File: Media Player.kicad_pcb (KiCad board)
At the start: 4 copper layers, 114.3 x 68.5 mm, 142 parts, among them J1 USB_C_Receptacle_USB2.0_16P, J10 MEM2075-00-140-01-A, J40 PH2.0, J41 UART, J70 SJ-3524-SMT-TR, Q10 DMP3068L-7, Q40 DMP3068L-7, Q50 DMP3068L-7, Q70 DMP3068L-7, SW30 BOOT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

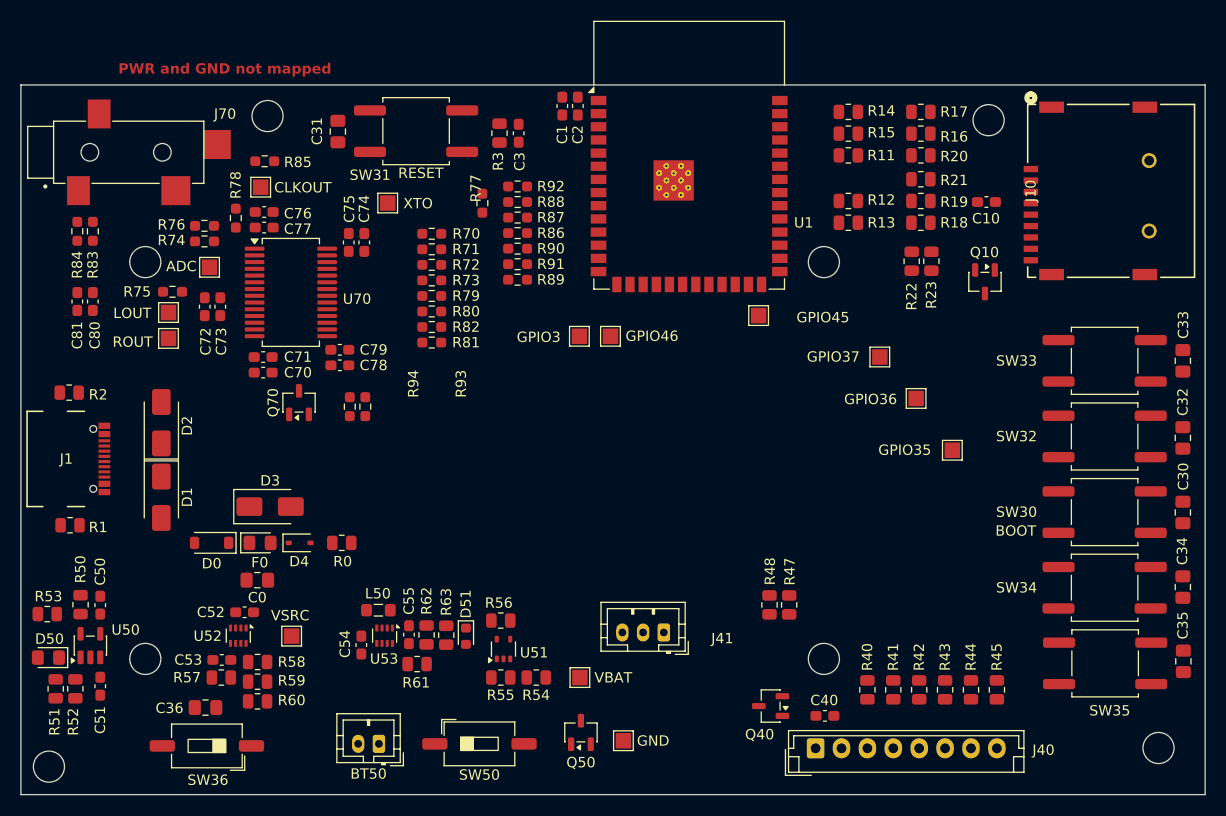
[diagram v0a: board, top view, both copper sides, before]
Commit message: JLC Design restraints
Updated design rules with JLC PCB. Combined numbers from Phils Lab and GPT for beginner friendly values (first board)
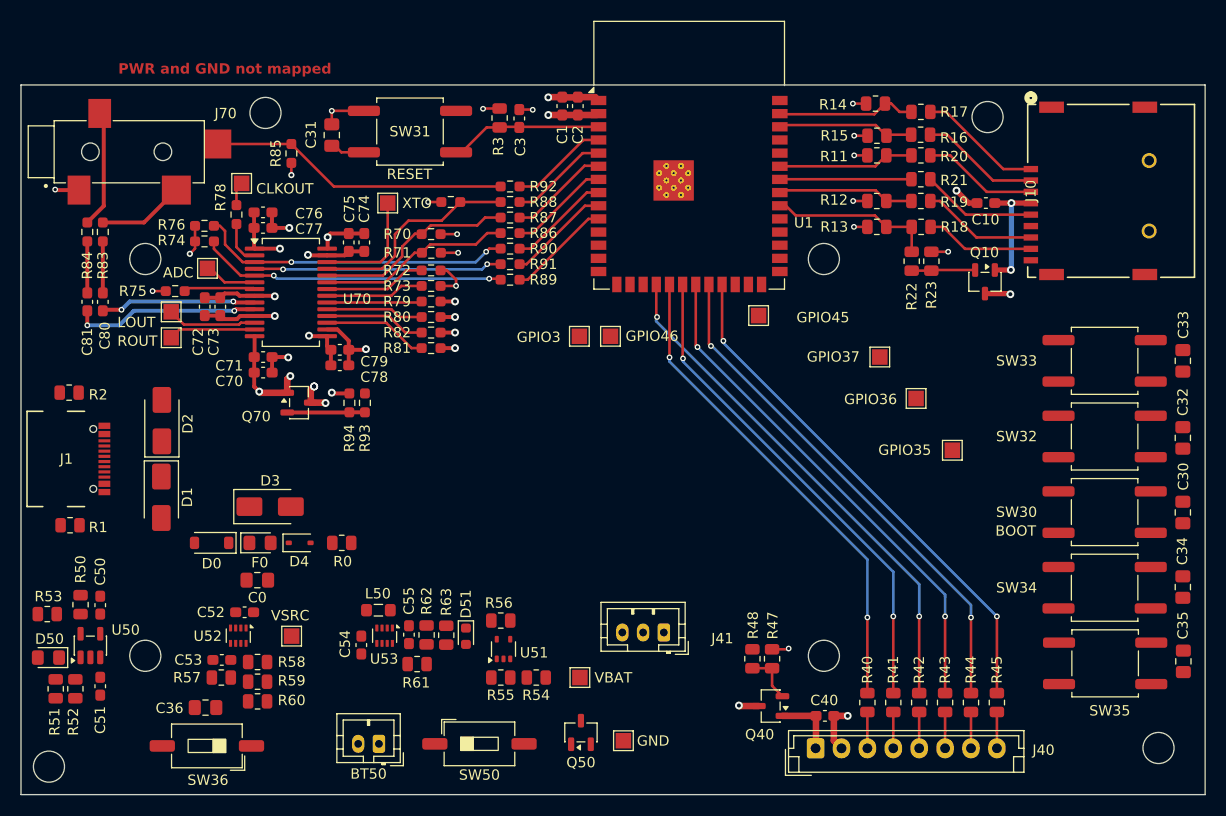
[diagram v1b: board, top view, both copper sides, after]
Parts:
- J1: value USB_C_Receptacle_USB2.0_16P -> 12402012E212A
- moved R47 5.46 mm to (158.7, 95.4)
- moved R48 5.46 mm to (156.8, 95.4)
- moved R77 3.05 mm to (127.7, 51.3), turned to 180 degrees
- moved R13 2.78 mm to (168.8, 53.7)
- moved R15 2.77 mm to (168.8, 44.9)
- moved R11 2.75 mm to (168.8, 46.8)
- moved R12 2.75 mm to (168.8, 51.2)
- moved R14 2.74 mm to (168.7, 41.8)
- moved R85 2.68 mm to (112.3, 46.6), turned to -90 degrees
- moved TP70 1.87 mm to (107.5, 49.5)
- moved R3 1.46 mm to (132.4, 43.2)
- moved C3 1.43 mm to (134.3, 43.2)
- moved R40 1.22 mm to (167.9, 99.6)
- moved R41 1.22 mm to (170.4, 99.6)
- moved R42 1.22 mm to (172.9, 99.6)
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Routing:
- net GND: track 0.00 -> 58.5 mm, vias 0 -> 19
- net /LCD_BL: track 0.00 -> 50.5 mm, vias 0 -> 2
- net /LCD_RST_n: track 0.00 -> 50.0 mm, vias 0 -> 2
- net /LCD_CS_n: track 0.00 -> 49.9 mm, vias 0 -> 2
- net /LCD_DS: track 0.00 -> 49.4 mm, vias 0 -> 2
- net /LCD_CLK: track 0.00 -> 47.9 mm, vias 0 -> 2
- net /LCD_DIN: track 0.00 -> 47.4 mm, vias 0 -> 2
- net /AudioAlt/A2_BCLK: track 0.00 -> 30.4 mm, vias 0 -> 2
- net /AudioAlt/A2_DACLRC: track 0.00 -> 29.6 mm, vias 0 -> 2
- net /AudioAlt/A2_TSW: track 0.00 -> 29.0 mm
- net /AudioAlt/AVDD: track 0.00 -> 28.6 mm, vias 0 -> 5
- net /AudioAlt/A2_DACDAT: track 0.00 -> 24.0 mm, vias 0 -> 2
- net +3V3: track 0.00 -> 23.9 mm, vias 0 -> 14
- net /AudioAlt/A2_MCLK: track 0.00 -> 20.7 mm
- net /AudioAlt/A2_SCLK: track 0.00 -> 19.6 mm
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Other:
- outline, holes or cut-outs redrawn
- board text added: "AVDD Area"
- board text added: "Am i allowed to do this? Decap is reached AFTER the pwr pin"
- board text added: "Avoid silk screen on via"
- board text added: "Design Rules are a combination of JLC, PhilsLab, and GPT values"
- board text added: "Make sure sd card signal length are +-50 mil"
- board text added: "VMID Area"
- board text added: "change size"
- board text added: "check recommended layout"

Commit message: Bucked
The Boost Buck Converter layout is from the datasheet. I'm not really sure how many via's I'll need for power since the IC is so small yet its the only source of power feeding all the other peripherals.
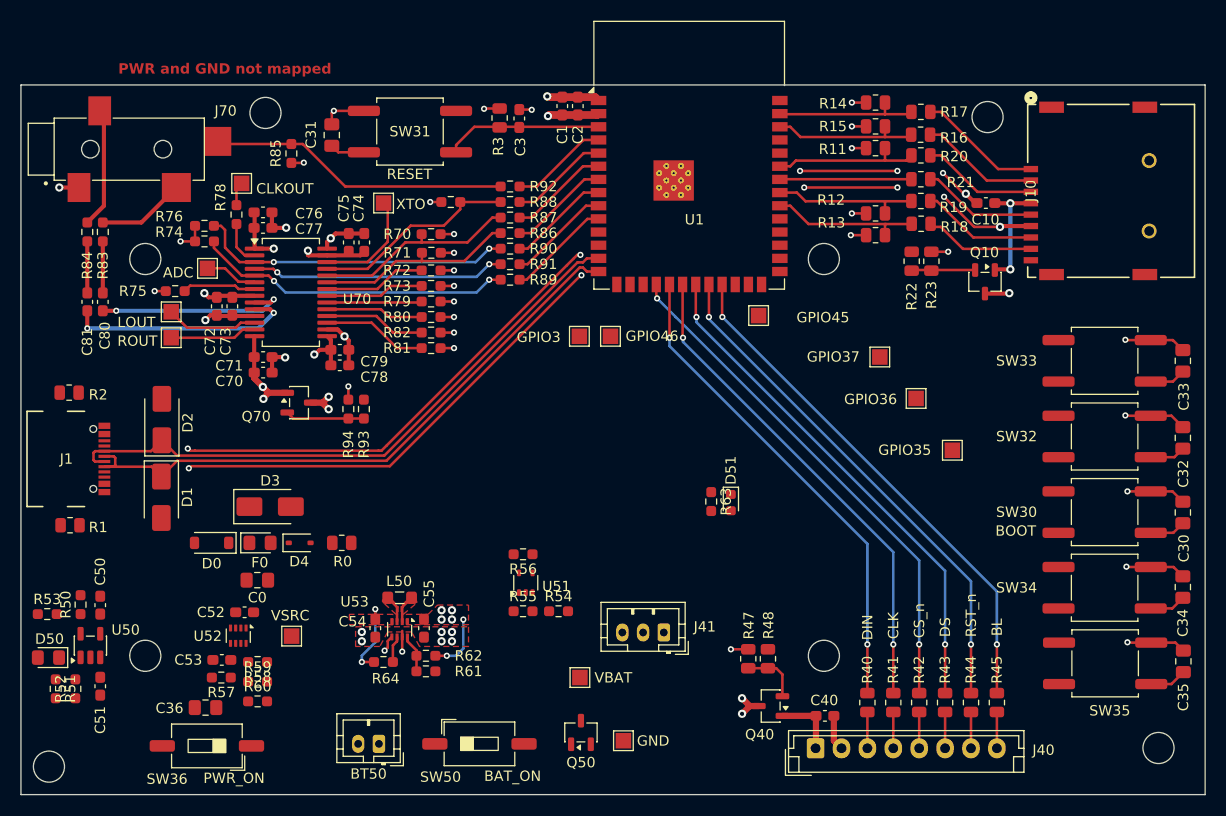
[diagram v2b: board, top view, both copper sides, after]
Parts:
- added R64: 10kΩ, Resistor_SMD:R_0603_1608Metric_Pad0.98x0.95mm_HandSolder, F.Cu at (121.2, 95.7)
- R50, R51, R52, R53, R54, R55, R56, R57, R58, R59, R60, R61, R62, R63: footprint Resistor_SMD:R_0805_2012Metric -> Resistor_SMD:R_0603_1608Metric_Pad0.98x0.95mm_HandSolder
- moved D51 28.6 mm to (154.7, 80.3)
- moved R63 28.6 mm to (152.8, 80.2)
- moved R54 6.75 mm to (138.1, 90.8)
- moved R55 6.75 mm to (134.7, 90.8)
- moved R56 6.75 mm to (134.7, 85.3)
- moved U51 6.75 mm to (134.9, 88.0)
- moved L50 2.38 mm to (122.8, 89.5)
- moved R47 2.30 mm to (156.4, 95.4)
- moved C54 2.11 mm to (120.4, 92.4)
- moved R62 2.01 mm to (125.3, 95.1), turned to 180 degrees
- moved C55 1.58 mm to (125.1, 92.4)
- moved U53 1.58 mm to (122.8, 92.5)
- moved R48 1.50 mm to (158.3, 95.4)
- moved R12 1.21 mm to (168.7, 52.4)
- moved C72 1.16 mm to (105.1, 61.4)
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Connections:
- net Net-(U53-LX1) renamed /Power/LX1
- net Net-(U53-LX2) renamed /Power/LX2
- C55 pad 1: +3.3V -> +3V3
- R62 pad 1: +3.3V -> +3V3
- R63 pad 1: +3.3V -> +3V3
- U51 pad 5: +3.3V -> +3V3
- U53 pad 1: +3.3V -> +3V3
- U53 pad 6: VSRC -> Net-(U53-MODE)
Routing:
- net GND: track 58.5 -> 204.4 mm, vias 19 -> 42
- net /USB_D-: track 0.00 -> 59.6 mm
- net /USB_D+: track 0.00 -> 59.5 mm
- net VSRC: track 0.00 -> 7.79 mm, vias 0 -> 2
- net +3V3: track 23.9 -> 30.1 mm, vias 14 -> 20
- net /AudioAlt/RHPOUT: track 18.2 -> 22.3 mm
- net /AudioAlt/LHPOUT: track 15.1 -> 18.9 mm
- net Net-(U53-FB): track 0.00 -> 3.68 mm
- net /PB3: track 0.00 -> 3.58 mm
- net /PB2: track 0.00 -> 3.52 mm
- net /PB1: track 0.00 -> 3.50 mm
- net /GPIO0: track 0.00 -> 3.48 mm
- net /AudioAlt/AVDD: track 28.6 -> 25.1 mm
- net /PB0: track 0.00 -> 3.44 mm
- net /Power/LX2: track 0.00 -> 2.67 mm
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- added copper zone on F.Cu, net +3V3
- added copper zone on F.Cu, net /Power/LX1
- added copper zone on F.Cu, net /Power/LX2
- added copper zone on F.Cu, net GND
- added copper zone on In1.Cu, net GND
- added copper zone on F.Cu, net VSRC
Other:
- board text added: "BAT_ON"
- board text added: "BL"
- board text added: "CLK"
- board text added: "CS_n"
- board text added: "DIN"
- board text added: "DS"
- board text added: "ESP asked to keep GND traces aroudn CLK, but this part near the pin also has 3v3"
- board text added: "PWR_ON"
- board text added: "RST_n"
- board text added: "Should each decap use it's own GND via?"
- board text added: "check for requirements surrounding GND and CLK"
- board text removed: "change size"

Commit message: Ideal Diode
Layout based on ds
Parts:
- moved D51 30.0 mm to (128.3, 94.5), turned to 0 degrees
- moved R63 27.5 mm to (128.4, 92.9), turned to 0 degrees
- moved C0 13.6 mm to (122.2, 84.3)
- moved J41 12.2 mm to (151.3, 104.7)
- moved R57 7.14 mm to (103.2, 90.5), turned to 0 degrees
- moved R55 5.22 mm to (135.8, 95.9)
- moved R56 5.22 mm to (135.8, 90.4)
- moved R54 5.22 mm to (139.2, 95.9)
- moved U51 5.22 mm to (136.0, 93.2)
- moved TP51 5.21 mm to (139.2, 103.7)
- moved Q50 5.21 mm to (135.1, 102.8)
- moved BT50 4.06 mm to (116.7, 103.8)
- moved SW50 4.06 mm to (126.4, 103.8)
- moved TP50 2.94 mm to (139.3, 100.0)
- moved C54 2.34 mm to (118.5, 93.8)
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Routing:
- net +3V3: track 30.1 -> 25.4 mm, vias 20 -> 19
- net Net-(U52-ST): track 0.00 -> 3.43 mm
- net /PWR_SRC: track 0.00 -> 2.77 mm, vias 0 -> 1
- net /PWR_ON_n: track 0.00 -> 2.02 mm
- net VSRC: track 7.79 -> 9.27 mm
- net GND: track 204.4 -> 205.7 mm, vias 42 -> 49
- added copper zone on F.Cu, net VBAT
- added copper zone on F.Cu, net VBUS

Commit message: Layout Draft 2, or almost
Charger layout based off of reference. Used more copper regions rather than traces. Other traces like buttons and test pads routed. Tried my best to make it all look good and parallel.

Added more silkscreen and logo.

STILL NEED TO DO POWER PLANE.
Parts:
- added G***: LOGO, Footprints:logo, F.Cu at (149.8, 79.7)
- moved TP7 16.1 mm to (142.2, 67.8)
- moved C0 15.0 mm to (107.2, 83.8), turned to 90 degrees
- moved TP3 11.3 mm to (166.0, 70.2)
- moved TP5 9.48 mm to (160.5, 70.2)
- moved TP4 9.35 mm to (163.2, 70.2)
- moved D0 4.78 mm to (107.8, 80.6)
- moved D3 4.05 mm to (114.3, 80.6)
- moved R52 3.06 mm to (91.2, 99.5), turned to 0 degrees
- moved TP6 2.94 mm to (142.2, 62.2)
- moved R51 2.72 mm to (90.3, 93.8)
- moved SW36 2.40 mm to (104.9, 103.8)
- moved C36 2.40 mm to (104.8, 100.2)
- moved R77 2.36 mm to (125.8, 52.7), turned to 0 degrees
- moved R56 1.73 mm to (134.9, 91.9)
- moved C51 1.70 mm to (92.9, 95.2), turned to 0 degrees
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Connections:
- net Net-(BT50-+) renamed /Power/BAT+
- net Net-(D0-A) renamed /USB_PWR
- net Net-(D0-K) renamed /USB_PWR2
- net Net-(Q50-D) renamed /Power/PMOS_D
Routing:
- net /CHRG_STAT: track 0.00 -> 102.3 mm, vias 0 -> 3
- net /TXD0: track 0.00 -> 70.9 mm, vias 0 -> 1
- net /RXD0: track 0.00 -> 69.7 mm, vias 0 -> 1
- net /PWR_SRC: track 2.77 -> 65.4 mm, vias 1 -> 2
- net /PB1: track 3.50 -> 57.5 mm, vias 0 -> 4
- net /PB3: track 3.58 -> 56.8 mm, vias 0 -> 2
- net /PB2: track 3.52 -> 50.9 mm, vias 0 -> 2
- net /PB0: track 3.44 -> 44.2 mm, vias 0 -> 2
- net /GPIO0: track 3.48 -> 43.0 mm, vias 0 -> 2
- net GND: track 205.7 -> 229.9 mm, vias 49 -> 81
- net /Power/BB_EN: track 1.61 -> 24.3 mm, vias 1 -> 2
- net Net-(U1-IO45): track 0.00 -> 22.3 mm
- net Net-(U1-IO37): track 0.00 -> 20.3 mm, vias 0 -> 2
- net Net-(U1-IO35): track 0.00 -> 19.6 mm, vias 0 -> 2
- net Net-(U1-IO36): track 0.00 -> 19.1 mm, vias 0 -> 2
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- added copper zone on F.Cu, net /Power/BAT+
- added copper zone on F.Cu, net /Power/PMOS_D
- added copper zone on B.Cu, net /USB_PWR
- added copper zone on F.Cu, net /USB_PWR
- added copper zone on F.Cu, net /USB_PWR2
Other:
- board text added: "BCLK"
- board text added: "LHP"
- board text added: "LRCLK"
- board text added: "MCLK"
- board text added: "PSRAM"
- board text added: "RHP"
- board text added: "ROBIN YAN"
- board text added: "SDA"
- board text added: "SDIN"
- board text added: "SLCK"
- board text added: "STRAP"
- board text added: "electrium mobility"
- board text removed: "The PTC fuse diode pads are too small! Recall, this to support high amounts of current"
- board text removed: "These TVS are huge! Return to original component!"

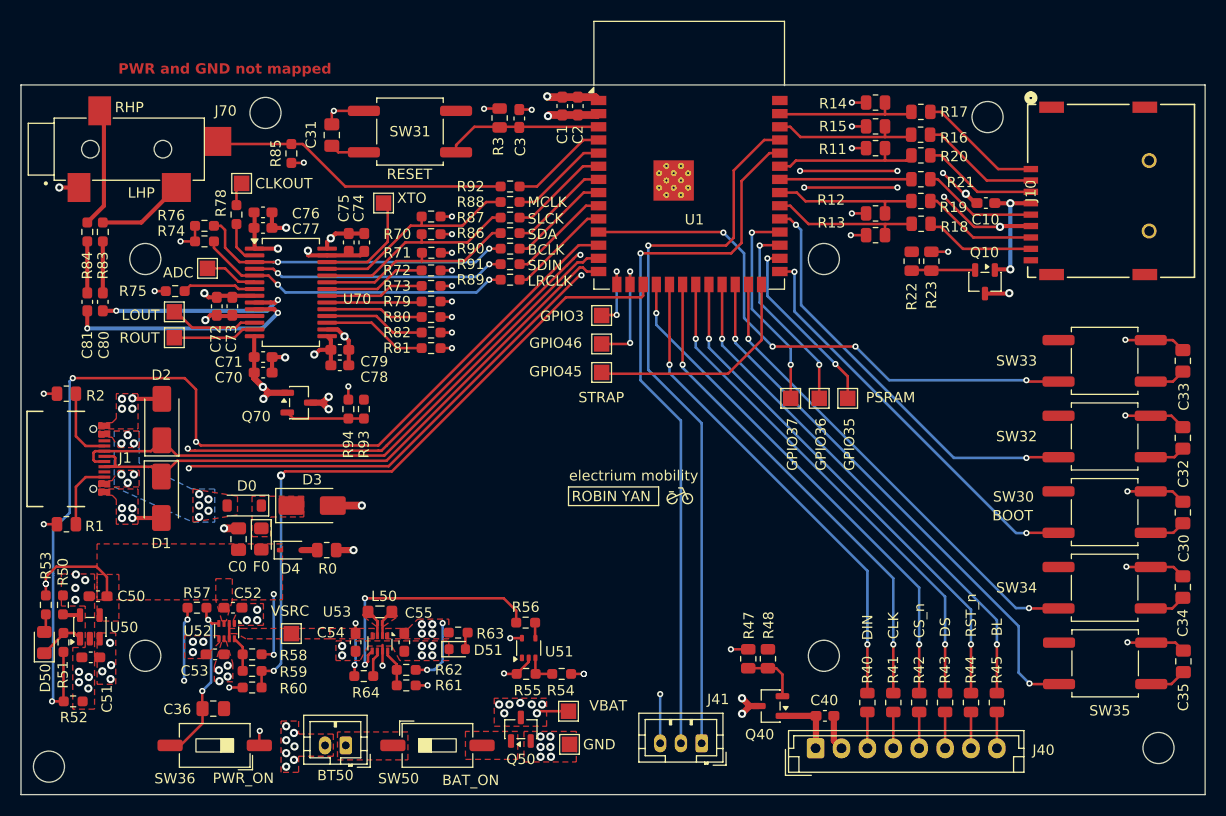
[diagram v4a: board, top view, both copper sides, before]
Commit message: Layout 2! Pre-DRC
32 DRC errors. 116 Warnings.

Inserted power planes. Now is time for optimization and fixing.
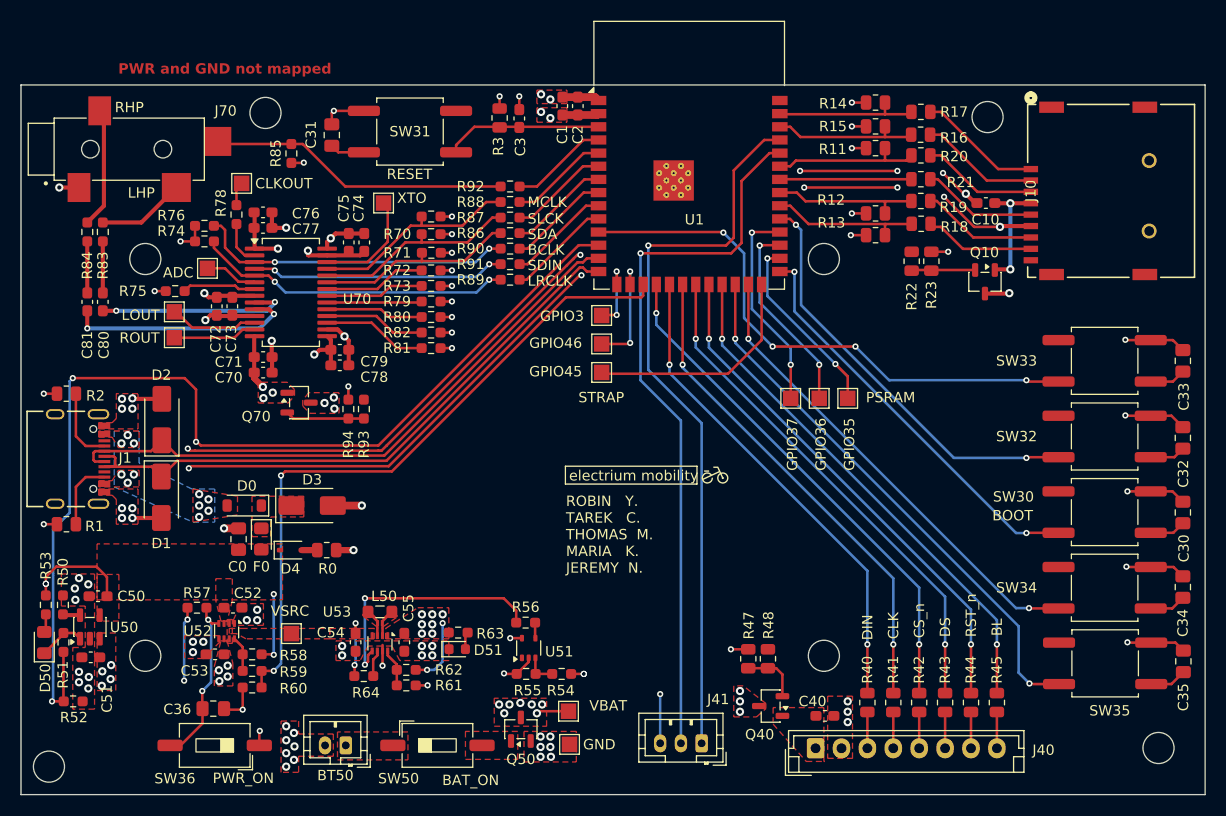
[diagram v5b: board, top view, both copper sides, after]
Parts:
- moved G*** 3.94 mm to (153.2, 77.7)
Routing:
- net +3V3: track 31.7 -> 24.1 mm, vias 21 -> 27
- net /LCD_VDD: track 6.38 -> 0.05 mm
- net /AudioAlt/AVDD: track 25.5 -> 22.1 mm, vias 5 -> 6
- net GND: track 229.9 -> 228.0 mm, vias 81 -> 91
- net VSRC: track 7.61 -> 6.13 mm
- net /AudioAlt/RHPOUT: track 23.1 -> 22.4 mm
- net /AudioAlt/LHPOUT: track 19.7 -> 19.0 mm
- net /Power/PMOS_D: vias 6 -> 0
- added copper zone on In2.Cu, net +3V3
- added copper zone on F.Cu, net /AudioAlt/AVDD
- added copper zone on In2.Cu, net /AudioAlt/AVDD
- added copper zone on In2.Cu, net /AudioAlt/VMID
- added copper zone on F.Cu, net /LCD_VDD
- added copper zone on In2.Cu, net VBAT
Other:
- board text added: "${REFERENCE}"
- board text added: "How many vias do I actually need for power to plane ?"
- board text added: "Is audio power plane ok? Many obstructions to direction power path"
- board text added: "Power pours/traces are small? Especially VSRC"
- board text added: "ROBIN Y. TAREK C. THOMAS M. MARIA K. JEREMY N."
- board text removed: "ROBIN YAN"
